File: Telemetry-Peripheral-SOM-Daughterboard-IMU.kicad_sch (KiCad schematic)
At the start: 3 parts, among them J1 Conn_02x10_Odd_Even

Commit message: very basic daughterboard
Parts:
- added C1, C2: 0.1u, Capacitor_SMD:C_0805_2012Metric, symbol Device:C_Small
- added U1: LSM6DSV, UTSVT_ICs:LGA14-L_2P59X3P1X0P5_STM, symbol utsvt-chips:LSM6DSV
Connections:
- net +3.3V: now also C1.1, C2.1, U1.5 (VDD_IO), U1.8 (VDD)
- net GND: now also C1.2, C2.2, U1.2 (SDX), U1.3 (SCX), U1.6 (GND), U1.7 (GND)
- net I2C2_SCL: now also U1.9 (INT2)
- net I2C2_SDA: now also U1.4 (INT1)
- net SPI1_MISO: now also U1.1 (SDO/SA0)
- net SPI1_MOSI: now also U1.14 (SDA)
- net SPI1_NSS: now also U1.12 (CS)
- net SPI1_SCK: now also U1.13 (SCL)
- no-connect marks 0 -> 9
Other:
- note added: "-IMU -SPI -2 programmable interrupts"
- note removed: "-fill in descriptions here!!"

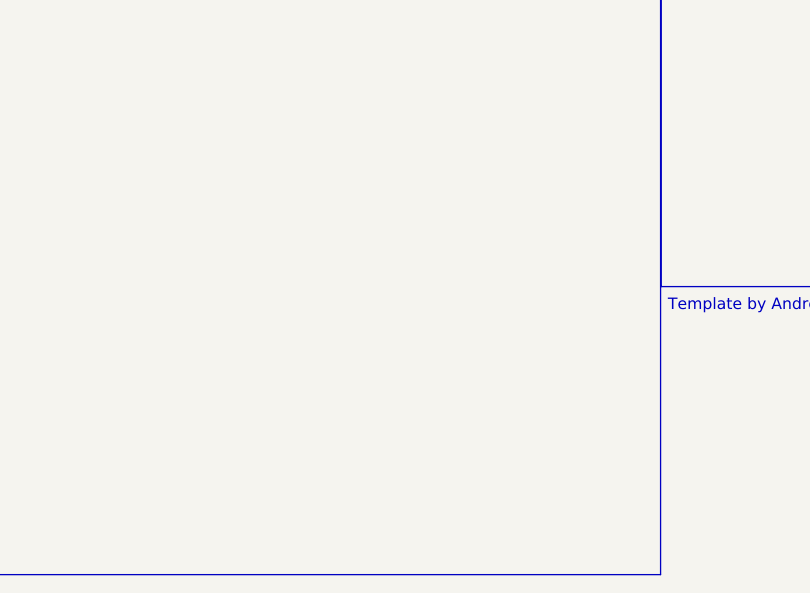
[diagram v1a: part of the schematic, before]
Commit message: created file for airflow sensor
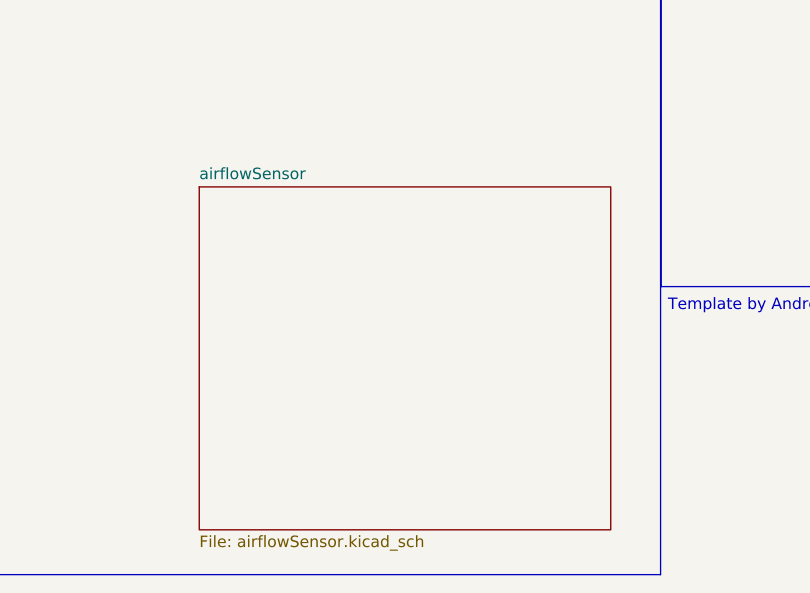
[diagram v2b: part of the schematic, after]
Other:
- added sheet airflowSensor (airflowSensor.kicad_sch)
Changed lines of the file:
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@@
+    )
+  )
+  (sheet (at 125.73 154.94) (size 45.72 38.1) (fields_autoplaced)
+    (stroke (width 0.1524) (type solid))
+    (fill (color 0 0 0 0.0000))
+    (property "Sheetname" "airflowSensor" (at 125.73 154.2284 0)
+      (effects (font (size 1.27 1.27)) (justify left bottom))
+    )
+    (property "Sheetfile" "airflowSensor.kicad_sch" (at 125.73 193.6246 0)
+      (effects (font (size 1.27 1.27)) (justify left top))
+    )
+    (instances
+      (project "Telemetry-Peripheral-SOM-Daughterboard-IMU"
+        (path "/637f68f0-cb9c-412a-8573-5d8e7ef6d8a2" (page "2"))
+      )
     )
   )

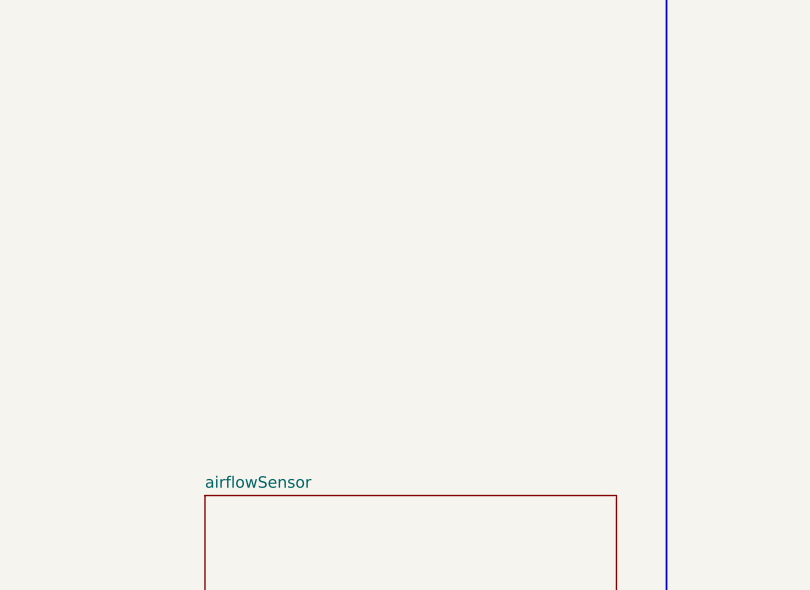
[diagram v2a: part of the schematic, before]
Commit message: created temperature sensor symbol and schematic
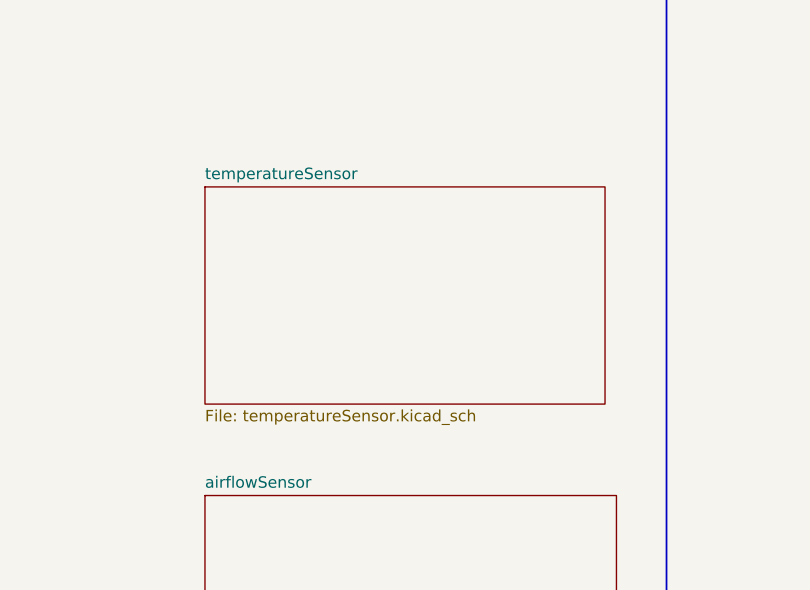
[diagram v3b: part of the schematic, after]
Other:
- added sheet temperatureSensor (temperatureSensor.kicad_sch)
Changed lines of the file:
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@@
+    )
+  )
+  (sheet (at 125.73 120.65) (size 44.45 24.13) (fields_autoplaced)
+    (stroke (width 0.1524) (type solid))
+    (fill (color 0 0 0 0.0000))
+    (property "Sheetname" "temperatureSensor" (at 125.73 119.9384 0)
+      (effects (font (size 1.27 1.27)) (justify left bottom))
+    )
+    (property "Sheetfile" "temperatureSensor.kicad_sch" (at 125.73 145.3646 0)
+      (effects (font (size 1.27 1.27)) (justify left top))
+    )
+    (instances
+      (project "Telemetry-Peripheral-SOM-Daughterboard-IMU"
+        (path "/637f68f0-cb9c-412a-8573-5d8e7ef6d8a2" (page "3"))
+      )
     )
   )

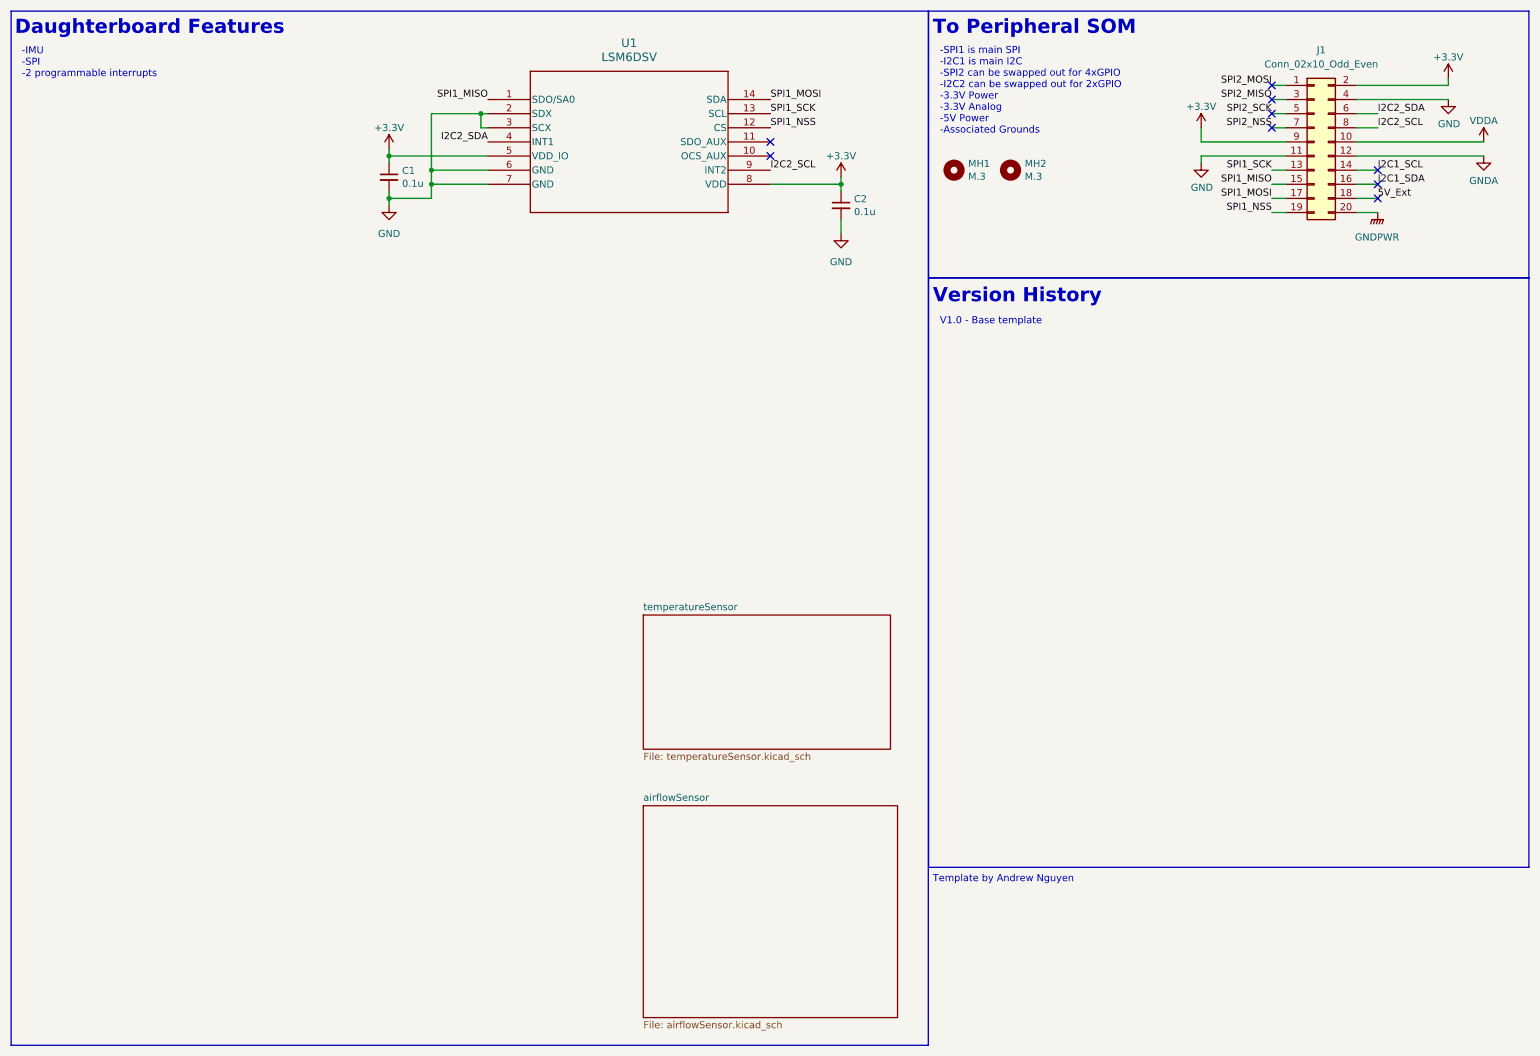
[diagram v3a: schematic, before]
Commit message: updated temperature sensor
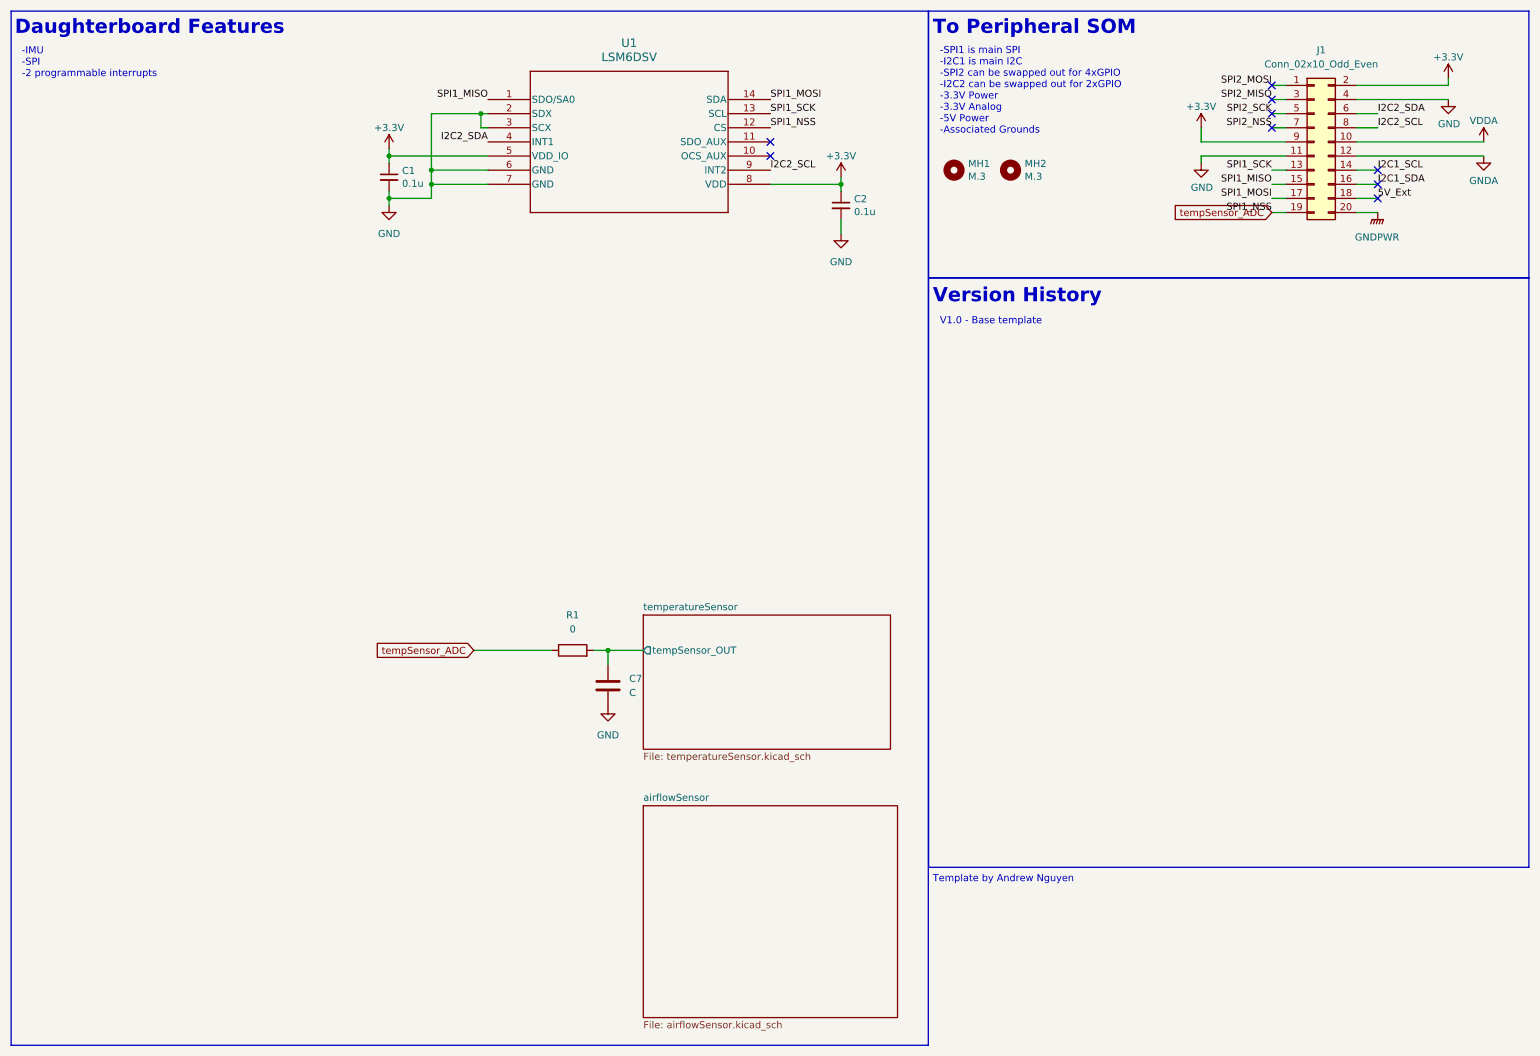
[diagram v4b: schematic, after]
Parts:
- added C7: C, symbol Device:C
- added R1: 0, symbol Device:R
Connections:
- net GND: now also C7.2
- net SPI1_NSS renamed tempSensor_ADC
- net tempSensor_ADC: now also R1.1
- new net temperatureSensor/tempSensor_OUT: C7.1, R1.2
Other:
- sheet temperatureSensor ports: added tempSensor_OUT; removed none
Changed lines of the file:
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@@
   (junction (at 87.63 40.64) (diameter 0) (color 0 0 0 0)
+  )
+  (junction (at 119.38 127) (diameter 0) (color 0 0 0 0)
   )
   (junction (at 80.01 38.1) (diameter 0) (color 0 0 0 0)
@@
     (stroke (width 0) (type default))
   )
+  (wire (pts (xy 119.38 127) (xy 119.38 129.54))
+    (stroke (width 0) (type default))
+  )
   (wire (pts (xy 254 45.72) (xy 257.81 45.72))
     (stroke (width 0) (type default))
@@
     (stroke (width 0) (type default))
   )
+  (wire (pts (xy 116.84 127) (xy 119.38 127))
+    (stroke (width 0) (type default))
+  )
   (wire (pts (xy 254 30.48) (xy 257.81 30.48))
     (stroke (width 0) (type default))
@@
   )
   (wire (pts (xy 254 43.18) (xy 257.81 43.18))
+    (stroke (width 0) (type default))
+  )
+  (wire (pts (xy 95.25 127) (xy 109.22 127))
+    (stroke (width 0) (type default))
+  )
+  (wire (pts (xy 119.38 127) (xy 125.73 127))
     (stroke (width 0) (type default))
   )
@@
     (effects (font (size 1.27 1.27)) (justify right bottom))
   )
+  (global_label "tempSensor_ADC" (shape input) (at 95.25 127 180) (fields_autoplaced)
+    (effects (font (size 1.27 1.27)) (justify right))
+    (property "Intersheetrefs" "${INTERSHEET_REFS}" (at 76.6016 127 0)
+      (effects (font (size 1.27 1.27)) (justify right) hide)
+    )
+  )
+  (global_label "tempSensor_ADC" (shape input) (at 238.76 48.26 180) (fields_autoplaced)
+    (effects (font (size 1.27 1.27)) (justify right))
+    (property "Intersheetrefs" "${INTERSHEET_REFS}" (at 220.1116 48.26 0)
+      (effects (font (size 1.27 1.27)) (justify right) hide)
+    )
+  )
   (symbol (lib_id "power:+3.3V") (at 80.01 36.83 0) (unit 1)
     (in_bom yes) (on_board yes) (dnp no) (fields_autoplaced)
@@
         (path "/d5ebd247-5a7c-47c2-8aee-beabaef72d6d"
           (reference "#PWR043") (unit 1)
+        )
+      )
+    )
+  )
+  (symbol (lib_id "Device:C") (at 119.38 133.35 0) (unit 1)
+    (in_bom yes) (on_board yes) (dnp no) (fields_autoplaced)
+    (property "Reference" "C7" (at 123.19 132.08 0)
+      (effects (font (size 1.27 1.27)) (justify left))
+    )
+    (property "Value" "C" (at 123.19 134.62 0)
+      (effects (font (size 1.27 1.27)) (justify left))
+    )
+    (property "Footprint" "" (at 120.3452 137.16 0)
+      (effects (font (size 1.27 1.27)) hide)
+    )
+    (property "Datasheet" "~" (at 119.38 133.35 0)
+      (effects (font (size 1.27 1.27)) hide)
+    )
+    (pin "1")
+    (pin "2")
+    (instances
+      (project "Telemetry-Peripheral-SOM-Daughterboard-IMU"
+        (path "/637f68f0-cb9c-412a-8573-5d8e7ef6d8a2"
+          (reference "C7") (unit 1)
         )
       )
@@
     )
   )
+  (symbol (lib_id "power:GND") (at 119.38 137.16 0) (unit 1)
+    (in_bom yes) (on_board yes) (dnp no) (fields_autoplaced)
+    (property "Reference" "#PWR017" (at 119.38 143.51 0)
+      (effects (font (size 1.27 1.27)) hide)
+    )
+    (property "Value" "GND" (at 119.38 142.24 0)
+      (effects (font (size 1.27 1.27)))
+    )
+    (property "Footprint" "" (at 119.38 137.16 0)
+      (effects (font (size 1.27 1.27)) hide)
+    )
+    (property "Datasheet" "" (at 119.38 137.16 0)
+      (effects (font (size 1.27 1.27)) hide)
+    )
+    (pin "1")
+    (instances
+      (project "Telemetry-Peripheral-SOM-Daughterboard-IMU"
+        (path "/637f68f0-cb9c-412a-8573-5d8e7ef6d8a2"
+          (reference "#PWR017") (unit 1)
+        )
+      )
+    )
+  )
   (symbol (lib_id "Device:C_Small") (at 80.01 41.91 0) (unit 1)
     (in_bom yes) (on_board yes) (dnp no)
@@
         (path "/d5ebd247-5a7c-47c2-8aee-beabaef72d6d"
           (reference "#PWR028") (unit 1)
+        )
+      )
+    )
+  )
+  (symbol (lib_id "Device:R") (at 113.03 127 90) (unit 1)
+    (in_bom yes) (on_board yes) (dnp no) (fields_autoplaced)
+    (property "Reference" "R1" (at 113.03 120.65 90)
+      (effects (font (size 1.27 1.27)))
+    )
+    (property "Value" "0" (at 113.03 123.19 90)
+      (effects (font (size 1.27 1.27)))
+    )
+    (property "Footprint" "" (at 113.03 128.778 90)
+      (effects (font (size 1.27 1.27)) hide)
+    )
+    (property "Datasheet" "~" (at 113.03 127 0)
+      (effects (font (size 1.27 1.27)) hide)
+    )
+    (pin "1")
+    (pin "2")
+    (instances
+      (project "Telemetry-Peripheral-SOM-Daughterboard-IMU"
+        (path "/637f68f0-cb9c-412a-8573-5d8e7ef6d8a2"
+          (reference "R1") (unit 1)
         )
       )
@@
       (effects (font (size 1.27 1.27)) (justify left top))
     )
-    (instances
+    (pin "tempSensor_OUT" output (at 125.73 127 180)
+      (effects (font (size 1.27 1.27)) (justify left))
+    )
+    (instances
